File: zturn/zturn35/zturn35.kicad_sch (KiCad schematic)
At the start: 45 parts, among them Q1 SSM6N15AFU, Q10 SSM6N15AFU, Q11 SSM6N15AFU, Q12 SSM6N15AFU, Q13 SSM6N15AFU, Q14 SSM6N15AFU, Q15 SSM6N15AFU, Q2 SSM6N15AFU, Q3 SSM6N15AFU, Q4 SSM6N15AFU, Q5 SSM6N15AFU, Q6 SSM6N15AFU, Q7 SSM6N15AFU, Q8 SSM6N15AFU, Q9 SSM6N15AFU, U10 74AXP4T245, U11 74AXP4T245, U12 74AXP4T245, U9 74AXP4T245

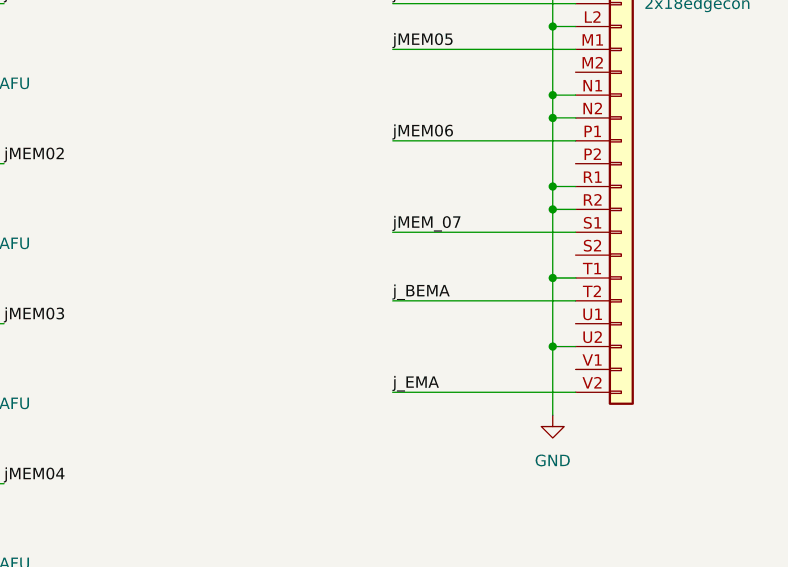
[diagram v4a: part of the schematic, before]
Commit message: update signals and zturn pcbs with pullups
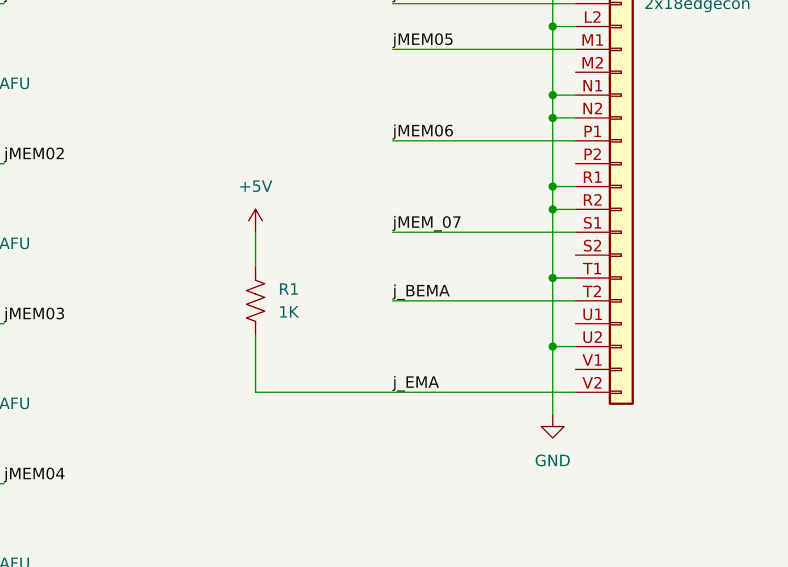
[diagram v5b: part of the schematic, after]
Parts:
- added R1: 1K, Resistor_THT:R_Axial_DIN0204_L3.6mm_D1.6mm_P5.08mm_Horizontal, symbol Device:R_US
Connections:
- net +5V: now also R1.1
- net j_EMA: now also R1.2
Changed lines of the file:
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@@
     (stroke (width 0) (type default))
   )
+  (wire (pts (xy 543.56 111.76) (xy 543.56 105.41))
+    (stroke (width 0) (type default))
+  )
   (wire (pts (xy 434.34 342.9) (xy 434.34 369.57))
     (stroke (width 0) (type default))
@@
     (stroke (width 0) (type default))
   )
-  (wire (pts (xy 558.8 111.76) (xy 579.12 111.76))
+  (wire (pts (xy 543.56 111.76) (xy 579.12 111.76))
     (stroke (width 0) (type default))
   )
@@
     (stroke (width 0) (type default))
   )
+  (wire (pts (xy 543.56 93.98) (xy 543.56 97.79))
+    (stroke (width 0) (type default))
+  )
   (wire (pts (xy 502.92 172.72) (xy 510.54 172.72))
     (stroke (width 0) (type default))
@@
     )
   )
+  (symbol (lib_id "power:+5V") (at 543.56 93.98 0) (unit 1)
+    (in_bom yes) (on_board yes) (dnp no) (fields_autoplaced)
+    (property "Reference" "#PWR03" (at 543.56 97.79 0)
+      (effects (font (size 1.27 1.27)) hide)
+    )
+    (property "Value" "+5V" (at 543.56 88.9 0)
+      (effects (font (size 1.27 1.27)))
+    )
+    (property "Footprint" "" (at 543.56 93.98 0)
+      (effects (font (size 1.27 1.27)) hide)
+    )
+    (property "Datasheet" "" (at 543.56 93.98 0)
+      (effects (font (size 1.27 1.27)) hide)
+    )
+    (pin "1")
+    (instances
+      (project "zturn35"
+        (path "/f88ff33f-ea83-4481-9378-71bec9a888d0"
+          (reference "#PWR03") (unit 1)
+        )
+      )
+    )
+  )
   (symbol (lib_id "mylibrary:SSM6N15AFU") (at 398.78 182.88 0) (unit 1)
     (in_bom yes) (on_board yes) (dnp no) (fields_autoplaced)
@@
         )
       )
+    )
+  )
+  (symbol (lib_id "Device:R_US") (at 543.56 101.6 0) (unit 1)
+    (in_bom yes) (on_board yes) (dnp no) (fields_autoplaced)
+    (property "Reference" "R1" (at 546.1 100.33 0)
+      (effects (font (size 1.27 1.27)) (justify left))
+    )
+    (property "Value" "1K" (at 546.1 102.87 0)
+      (effects (font (size 1.27 1.27)) (justify left))
+    )
+    (property "Footprint" "Resistor_THT:R_Axial_DIN0204_L3.6mm_D1.6mm_P5.08mm_Horizontal" (at 544.576 101.854 90)
+      (effects (font (size 1.27 1.27)) hide)
+    )
+    (property "Datasheet" "~" (at 543.56 101.6 0)
+      (effects (font (size 1.27 1.27)) hide)
+    )
+    (pin "1")
+    (pin "2")
+    (instances
+      (project "zturn35"
+        (path "/f88ff33f-ea83-4481-9378-71bec9a888d0"
+          (reference "R1") (unit 1)
+        )
+      )

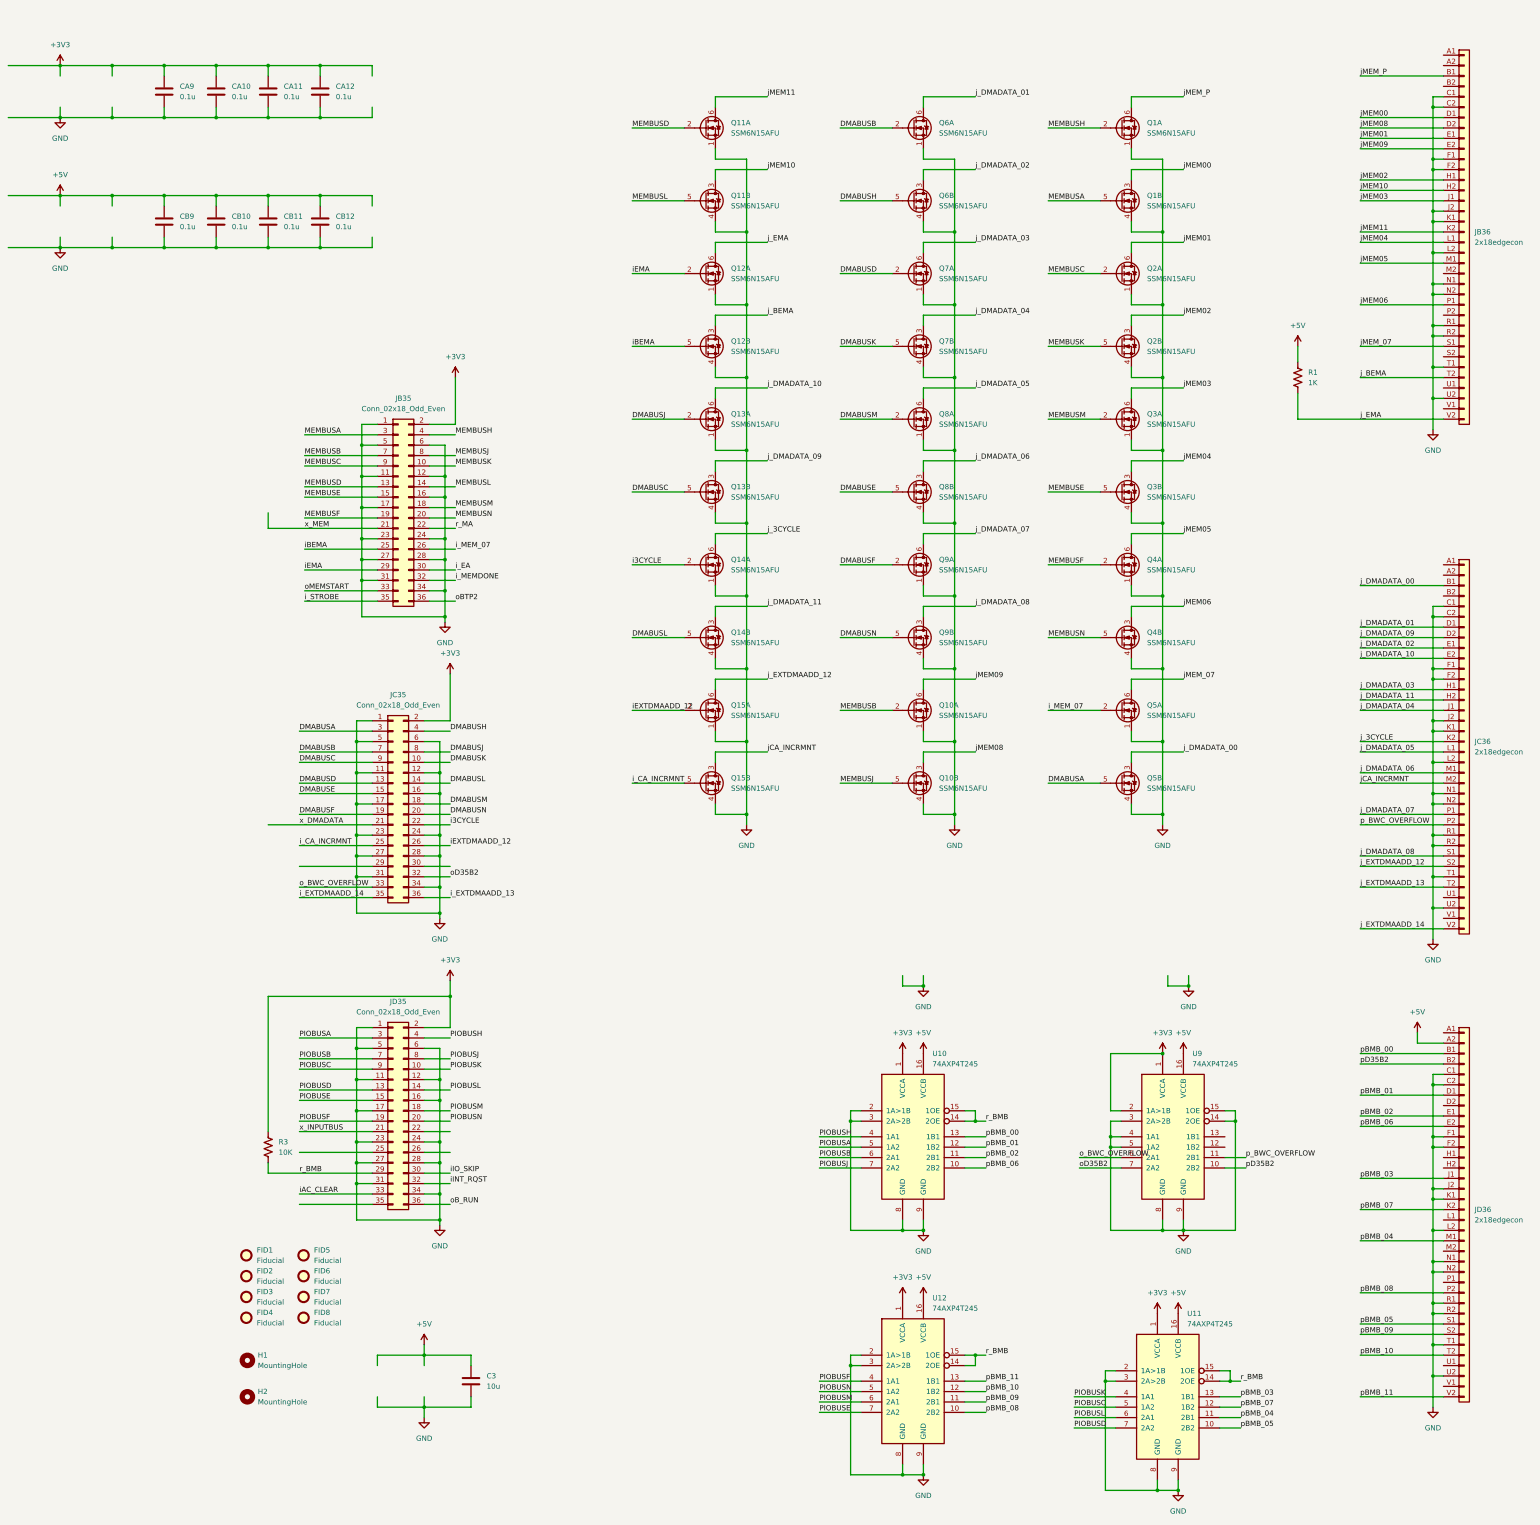
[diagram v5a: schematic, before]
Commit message: add I2C circuit to zturn boardset to operate front panel board
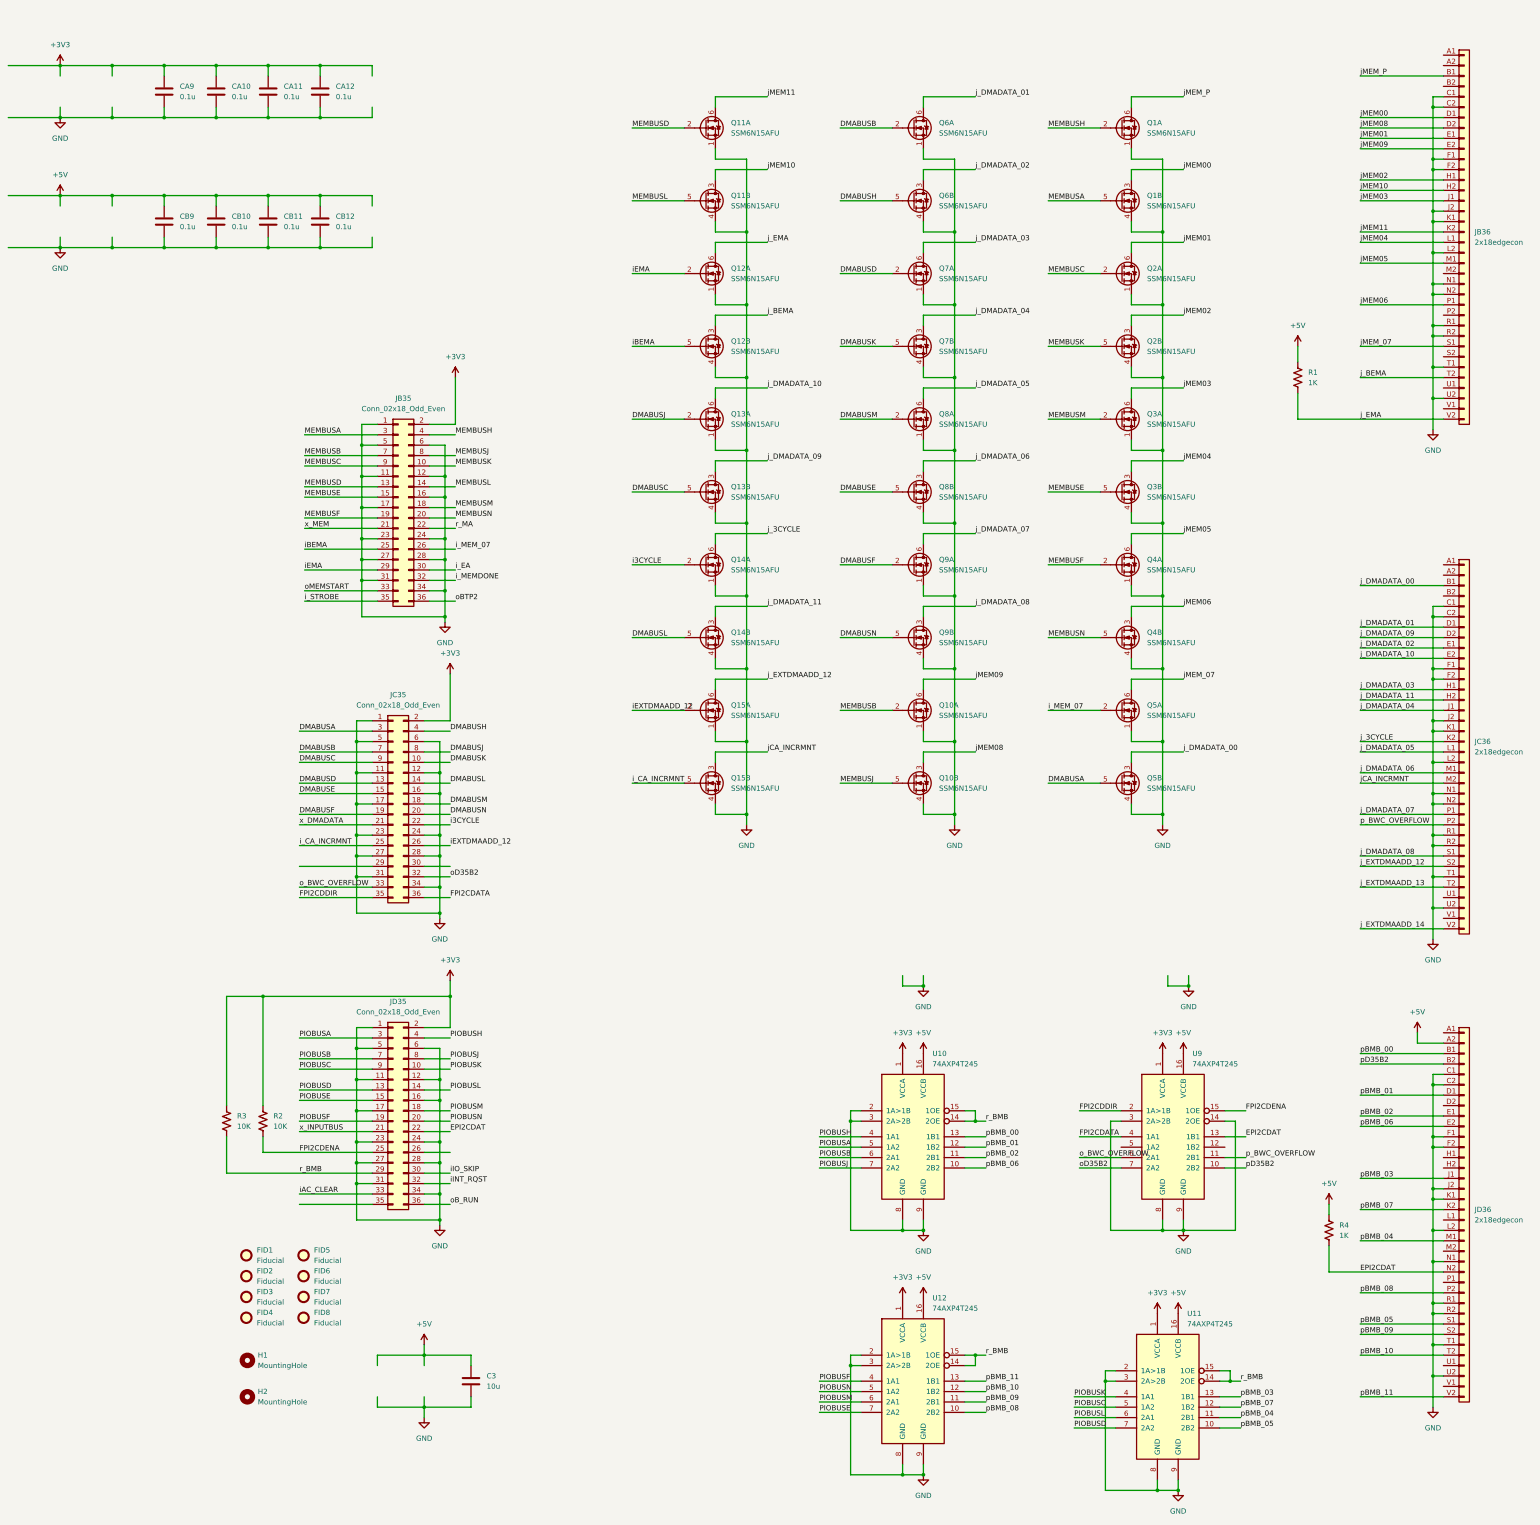
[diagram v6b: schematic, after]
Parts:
- added R2: 10K, Resistor_SMD:R_0201_0603Metric, symbol Device:R_US
- added R4: 1K, Resistor_THT:R_Axial_DIN0204_L3.6mm_D1.6mm_P5.08mm_Horizontal, symbol Device:R_US
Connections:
- net +3V3: now also R2.1; no longer U9.2 (1A>1B)
- net +5V: now also R4.1
- net GND: no longer JD36.N2, U9.15 (1OE), U9.4 (1A1), U9.5 (1A2)
- net EPI2CDAT: now reaches U9.13 (1B1)
- net EPI2CDAT: now also JD35.22 (Pin_22), JD36.N2, R4.2
- net FPI2CDENA: now reaches JD35.25 (Pin_25)
- net FPI2CDENA: now also U9.15 (1OE), R2.2
- net i_EXTDMAADD_13 renamed FPI2CDATA
- net FPI2CDATA: now also U9.4 (1A1)
- net i_EXTDMAADD_14 renamed FPI2CDDIR
- net FPI2CDDIR: now also U9.2 (1A>1B)
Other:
- moved on the sheet: R3

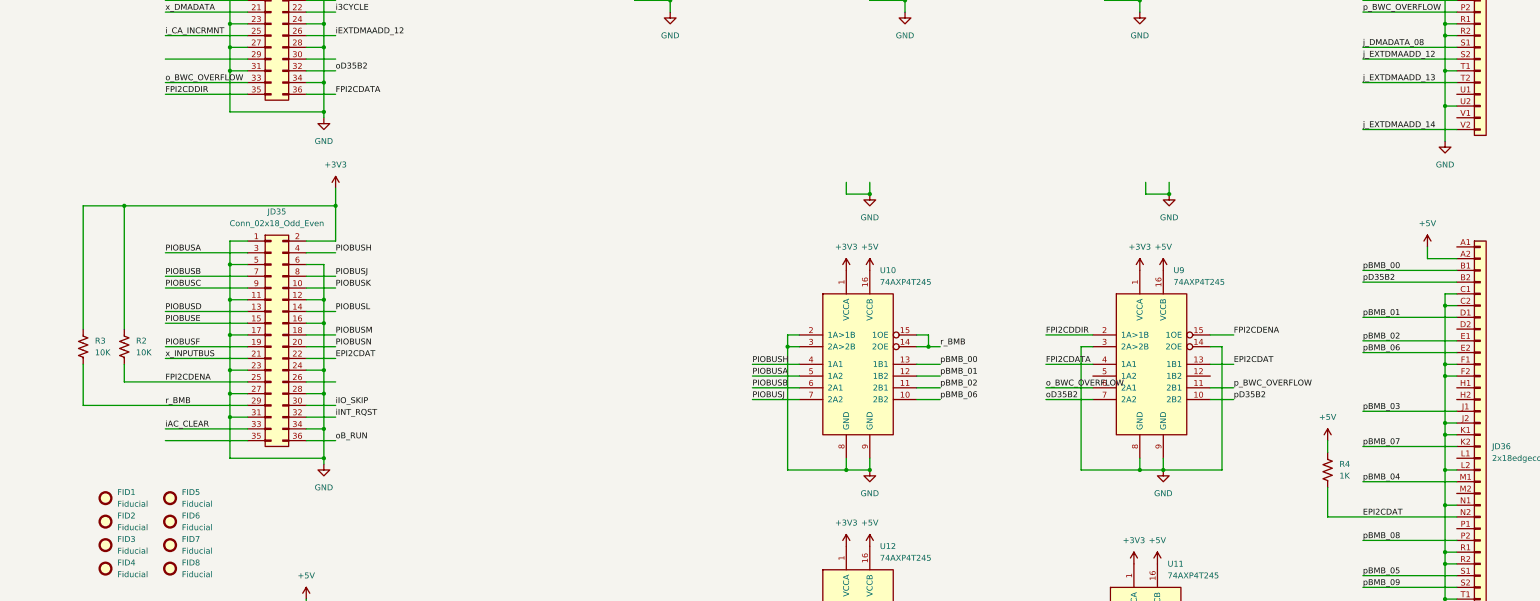
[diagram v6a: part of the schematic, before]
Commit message: update zturn36,35 pcbs to put i2c at 3.3V and open-collector
...directly from FPGA pins with 2.2K pullups
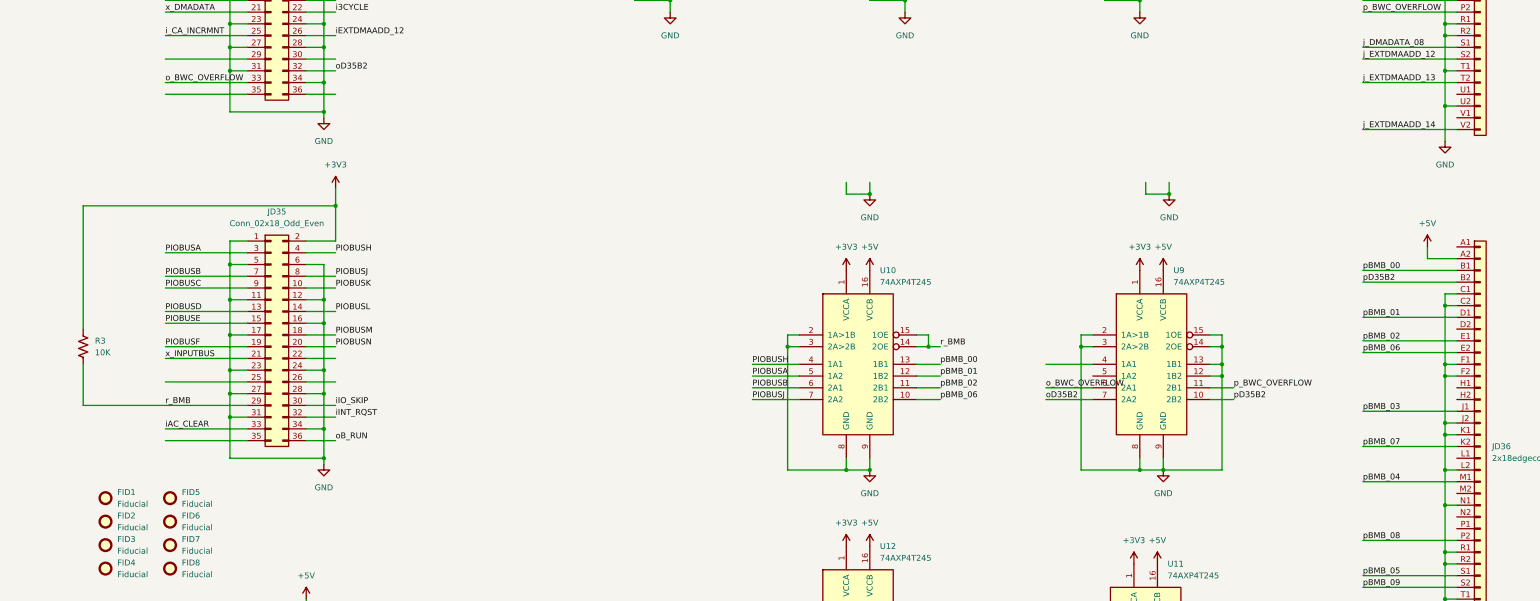
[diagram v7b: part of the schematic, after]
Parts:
- removed R2: 10K, Resistor_SMD:R_0201_0603Metric, symbol Device:R_US
- removed R4: 1K, Resistor_THT:R_Axial_DIN0204_L3.6mm_D1.6mm_P5.08mm_Horizontal, symbol Device:R_US
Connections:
- net GND: now also U9.12 (1B2), U9.13 (1B1), U9.15 (1OE), U9.2 (1A>1B)
- removed net EPI2CDAT: JD35.22 (Pin_22), JD36.N2, U9.13 (1B1)
- net FPI2CDATA: no longer names the net of U9.4 (1A1)
- net FPI2CDATA: no longer JC35.36 (Pin_36)
- net FPI2CDDIR: no longer names the net of JC35.35 (Pin_35)
- net FPI2CDDIR: no longer U9.2 (1A>1B)
- net FPI2CDENA: no longer names the net of JD35.25 (Pin_25)
- net FPI2CDENA: no longer U9.15 (1OE)

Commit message: put 2024-12-30 version of zturn35,36 boards back
the 2024-12-30 design had 5V I2C bus via 74AXP245s
the newer boards had 3.3V I2C bus directly on FPGA

the old boards work perfectly fine so go back to them
...rather than make new boards
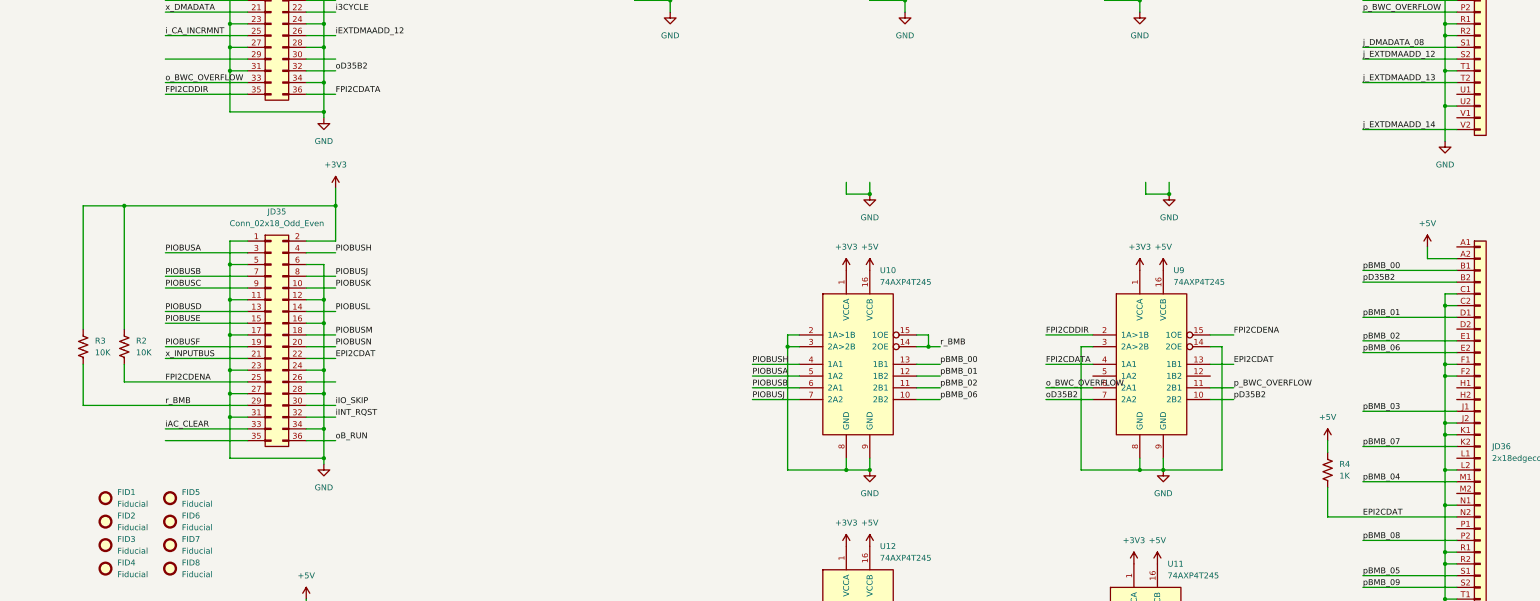
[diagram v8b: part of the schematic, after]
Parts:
- added R2: 10K, Resistor_SMD:R_0201_0603Metric, symbol Device:R_US
- added R4: 1K, Resistor_THT:R_Axial_DIN0204_L3.6mm_D1.6mm_P5.08mm_Horizontal, symbol Device:R_US
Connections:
- net +3V3: now also R2.1
- net +5V: now also R4.1
- net GND: no longer U9.12 (1B2), U9.13 (1B1), U9.15 (1OE), U9.2 (1A>1B)
- net FPI2CDATA: now reaches U9.4 (1A1)
- net FPI2CDATA: now also JC35.36 (Pin_36)
- net EPI2CDAT: now reaches JD36.N2
- net EPI2CDAT: now also JD35.22 (Pin_22), U9.13 (1B1), R4.2
- net FPI2CDENA: now reaches JD35.25 (Pin_25)
- net FPI2CDENA: now also U9.15 (1OE), R2.2
- net FPI2CDDIR: now reaches JC35.35 (Pin_35)
- net FPI2CDDIR: now also U9.2 (1A>1B)
